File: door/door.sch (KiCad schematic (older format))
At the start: 10 parts, among them J1 POWER, J2 CONTROL, J3 ENDPOINT, J4 MOTOR, Q1 IRF3205

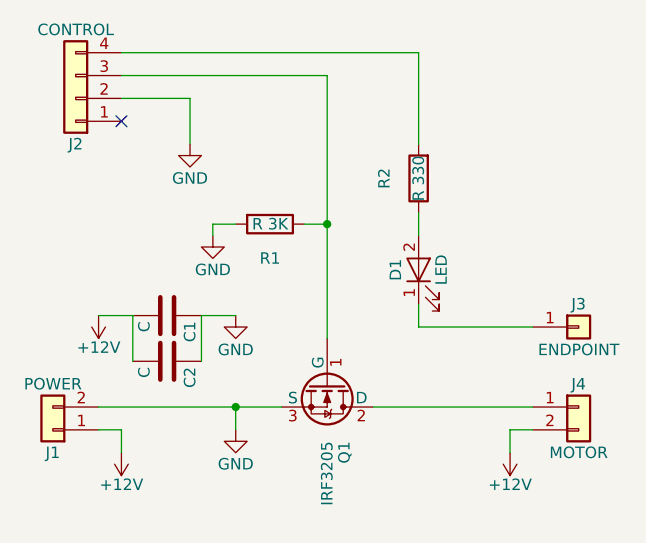
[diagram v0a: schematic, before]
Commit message: Made the door pcb half the size
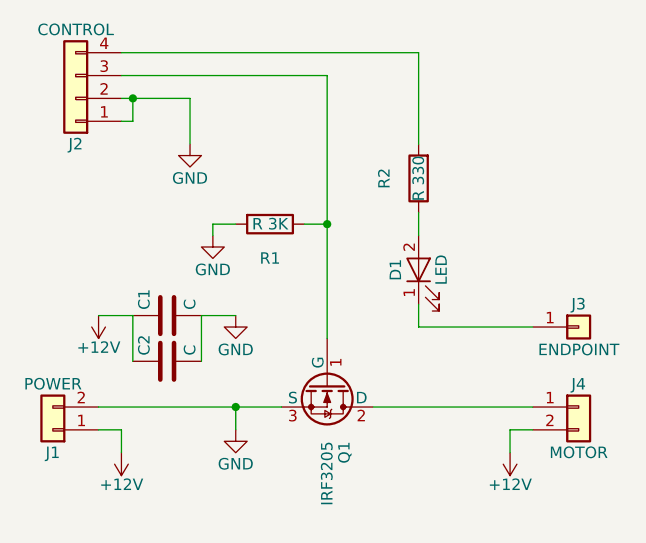
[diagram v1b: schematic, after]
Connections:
- net +12V: now also C1.1, C2.1; no longer C1.2, C2.2
- net GND: now also C1.2, C2.2, J2.1 (Pin_1); no longer C1.1, C2.1
- no-connect marks 1 -> 0
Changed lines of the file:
@@
 F 3 "" H 2450 2450 50  0001 C CNN
 	1    2450 2450
-	0    1    1    0
+	0    -1   -1   0
 $EndComp
 $Comp
@@
 F 3 "" H 2450 2250 50  0001 C CNN
 	1    2450 2250
-	0    1    1    0
+	0    -1   -1   0
 $EndComp
 $Comp
@@
 	1    0    0    -1
 $EndComp
-NoConn ~ 2250 1400
 $Comp
 L R R1
@@
 	-1   0    0    1
 $EndComp
+Wire Wire Line
+	2250 1400 2300 1400
+Wire Wire Line
+	2300 1400 2300 1300
+Connection ~ 2300 1300
 $EndSCHEMATC

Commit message: Added diode to the door signal
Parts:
- added D2: D, Resistors_SMD:R_0805_HandSoldering, symbol D
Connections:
- net at Q1.1 (G), R1.1: now also D2.1 (K); no longer J2.3 (Pin_3)
- new net: D2.2 (A), J2.3 (Pin_3)
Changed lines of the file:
@@
 $EndComp
 $Comp
-L GND #PWR6
+L GND #PWR01
 U 1 1 5A2C1DEC
 P 2750 2750
-F 0 "#PWR6" H 2750 2500 50  0001 C CNN
+F 0 "#PWR01" H 2750 2500 50  0001 C CNN
 F 1 "GND" H 2750 2600 50  0000 C CNN
 F 2 "" H 2750 2750 50  0001 C CNN
@@
 $EndComp
 $Comp
-L +12V #PWR2
+L +12V #PWR02
 U 1 1 5A2C1B7E
 P 2250 2850
-F 0 "#PWR2" H 2250 2700 50  0001 C CNN
+F 0 "#PWR02" H 2250 2700 50  0001 C CNN
 F 1 "+12V" H 2250 2990 50  0000 C CNN
 F 2 "" H 2250 2850 50  0001 C CNN
@@
 $EndComp
 $Comp
-L +12V #PWR7
+L +12V #PWR03
 U 1 1 5A2C1B54
 P 3950 2850
-F 0 "#PWR7" H 3950 2700 50  0001 C CNN
+F 0 "#PWR03" H 3950 2700 50  0001 C CNN
 F 1 "+12V" H 3950 2990 50  0000 C CNN
 F 2 "" H 3950 2850 50  0001 C CNN
@@
 $EndComp
 $Comp
-L GND #PWR3
+L GND #PWR04
 U 1 1 5A2BFE97
 P 2550 1500
-F 0 "#PWR3" H 2550 1250 50  0001 C CNN
+F 0 "#PWR04" H 2550 1250 50  0001 C CNN
 F 1 "GND" H 2550 1350 50  0000 C CNN
 F 2 "" H 2550 1500 50  0001 C CNN
@@
 $EndComp
 $Comp
-L GND #PWR4
+L GND #PWR05
 U 1 1 5A2C092E
 P 2650 1900
-F 0 "#PWR4" H 2650 1650 50  0001 C CNN
+F 0 "#PWR05" H 2650 1650 50  0001 C CNN
 F 1 "GND" H 2650 1750 50  0000 C CNN
 F 2 "" H 2650 1900 50  0001 C CNN
@@
 $EndComp
 $Comp
-L GND #PWR5
+L GND #PWR06
 U 1 1 5A2C02A9
 P 2750 2250
-F 0 "#PWR5" H 2750 2000 50  0001 C CNN
+F 0 "#PWR06" H 2750 2000 50  0001 C CNN
 F 1 "GND" H 2750 2100 50  0000 C CNN
 F 2 "" H 2750 2250 50  0001 C CNN
@@
 $EndComp
 $Comp
-L +12V #PWR1
+L +12V #PWR07
 U 1 1 5A2C1E37
 P 2150 2250
-F 0 "#PWR1" H 2150 2100 50  0001 C CNN
+F 0 "#PWR07" H 2150 2100 50  0001 C CNN
 F 1 "+12V" H 2150 2390 50  0000 C CNN
 F 2 "" H 2150 2250 50  0001 C CNN
@@
 Wire Wire Line
 	2650 1850 2750 1850
-Wire Wire Line
-	3150 1200 3150 2350
 Wire Wire Line
 	3050 1850 3150 1850
@@
 	2300 1400 2300 1300
 Connection ~ 2300 1300
+$Comp
+L D D2
+U 1 1 5A2D9211
+P 3150 1450
+F 0 "D2" H 3150 1550 50  0000 C CNN
+F 1 "D" H 3150 1350 50  0000 C CNN
+F 2 "Resistors_SMD:R_0805_HandSoldering" H 3150 1450 50  0001 C CNN
+F 3 "" H 3150 1450 50  0001 C CNN
+	1    3150 1450
+	0    -1   -1   0
+$EndComp
+Wire Wire Line
+	3150 1200 3150 1300
+Wire Wire Line
+	3150 1600 3150 2350
 $EndSCHEMATC
